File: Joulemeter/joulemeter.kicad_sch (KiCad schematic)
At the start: 42 parts, among them IC1 INA240A3PWR, J1 XT60-M, J2 XT60-M, J3 22035035, J4 22035035, U2 MCP6286T-E/OT, U5 PADS131M04QPWRQ1

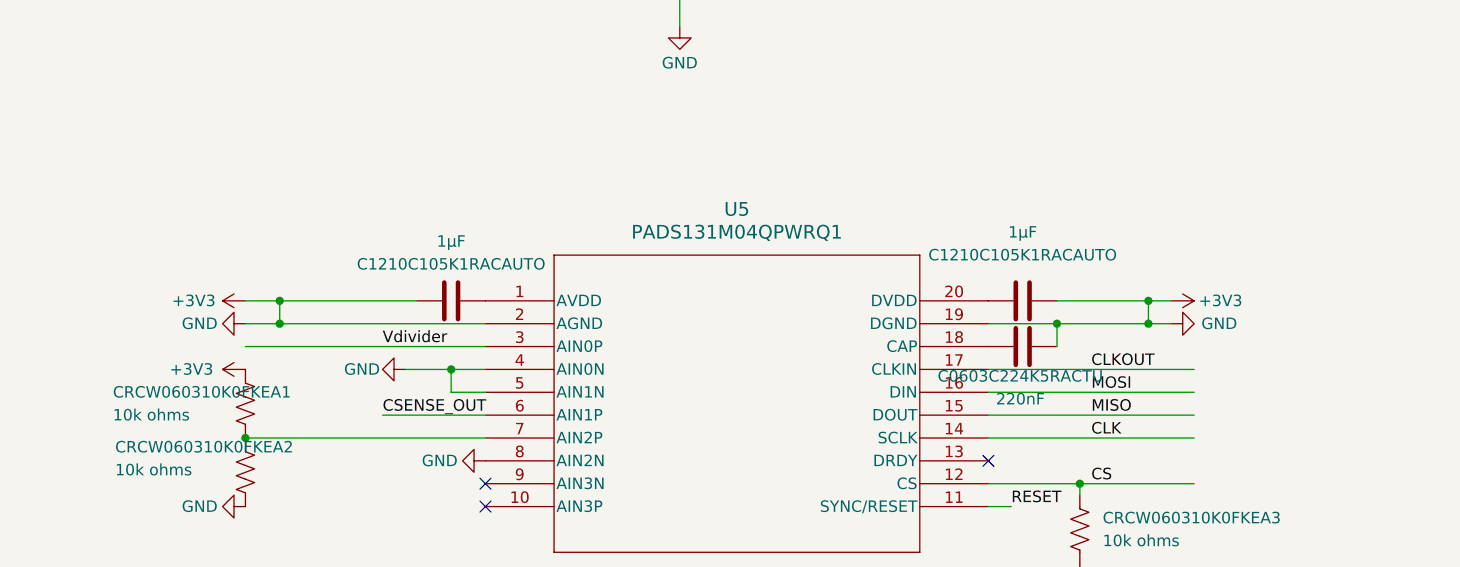
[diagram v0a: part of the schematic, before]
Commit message: fixed avdd agnd dvdd dgnd connections
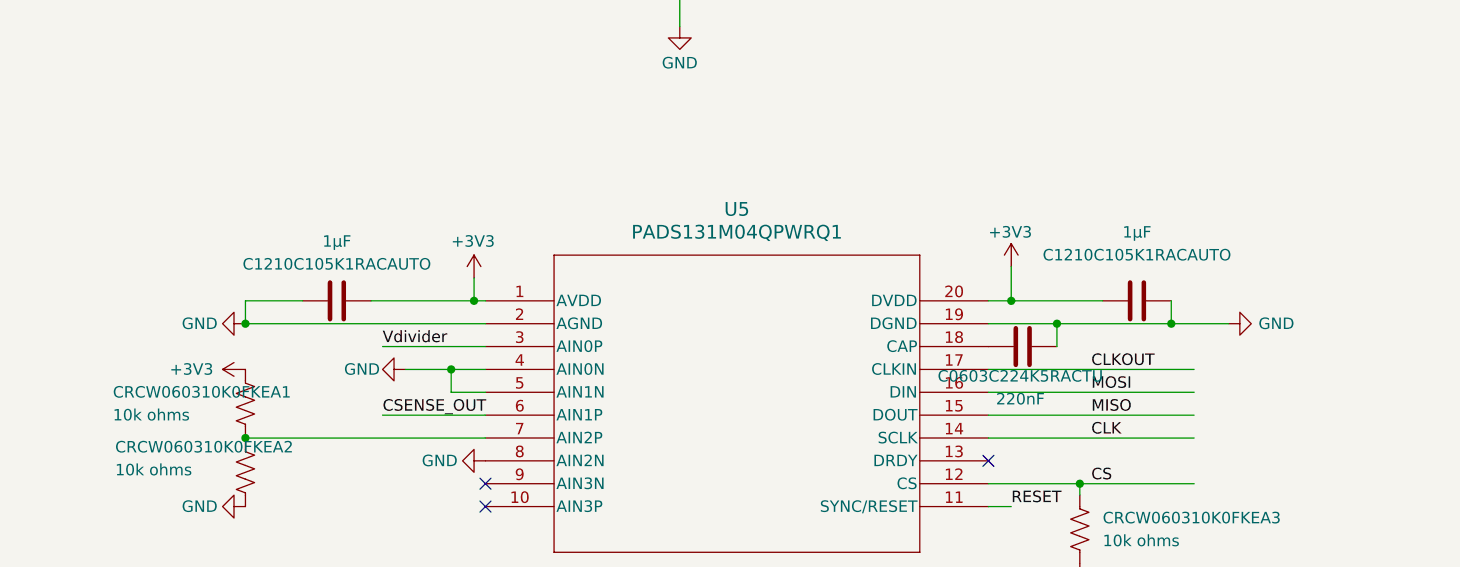
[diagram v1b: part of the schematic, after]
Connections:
- net +3V3: now also C1210C105K1RACAUTO.1, C1210C105K1RACAUTO.2, U5.1 (AVDD), U5.20 (DVDD); no longer C0603C224K5RACTU.2, C0603S223K5RACTU.1, C0805C475K4RACTU.2, C0805C475K4RACTU1.2, C1210C105K1RACAUTO.1, C1210C105K1RACAUTO.2, C1210C105K1RACAUTO.2, C1210C106K3RACAUTO.2, CRCW060310K0FKEA2.1, D1.1, IC1.4 (GND), IC1.7 (REF1), J1.N (NEG), J2.N (NEG), J3.2, J4.2, LDO1.4 (GND), RP2.13, RP2.2, TNPW080510K0BEEA.2, TP_GND.1, U2.2 (VSS), U5.19 (DGND), U5.2 (AGND), U5.4 (AIN0N), U5.5 (AIN1N), U5.8 (AIN2N)
- net GND: now reaches RP2.2
- net GND: now also C0603C224K5RACTU.2, C0603S223K5RACTU.1, C0805C475K4RACTU.2, C0805C475K4RACTU1.2, C1210C105K1RACAUTO.1, C1210C105K1RACAUTO.2, C1210C105K1RACAUTO.2, C1210C106K3RACAUTO.2, CRCW060310K0FKEA2.1, D1.1, IC1.4 (GND), IC1.7 (REF1), J1.N (NEG), J2.N (NEG), J3.2, J4.2, LDO1.4 (GND), RP2.13, TNPW080510K0BEEA.2, TP_GND.1, U2.2 (VSS), U5.19 (DGND), U5.2 (AGND), U5.4 (AIN0N), U5.5 (AIN1N), U5.8 (AIN2N)
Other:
- moved on the sheet: C1210C105K1RACAUTO

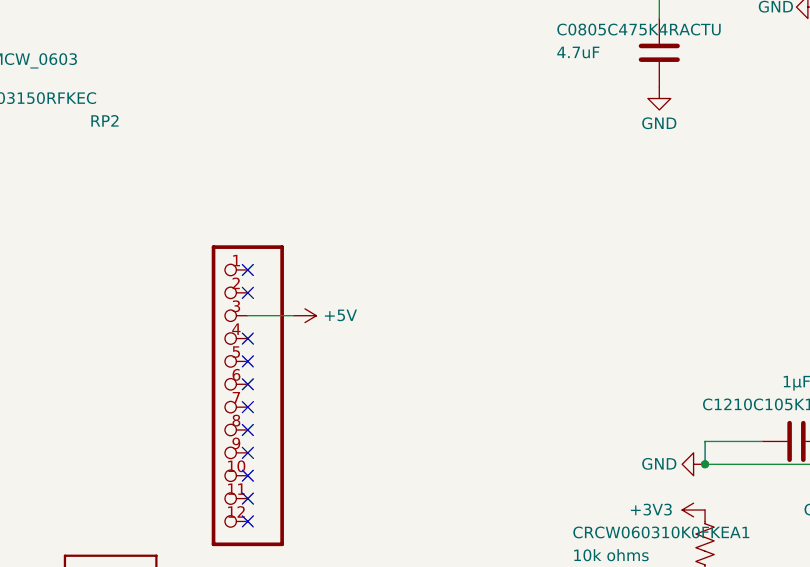
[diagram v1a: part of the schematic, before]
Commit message: bypass cap for rp2040
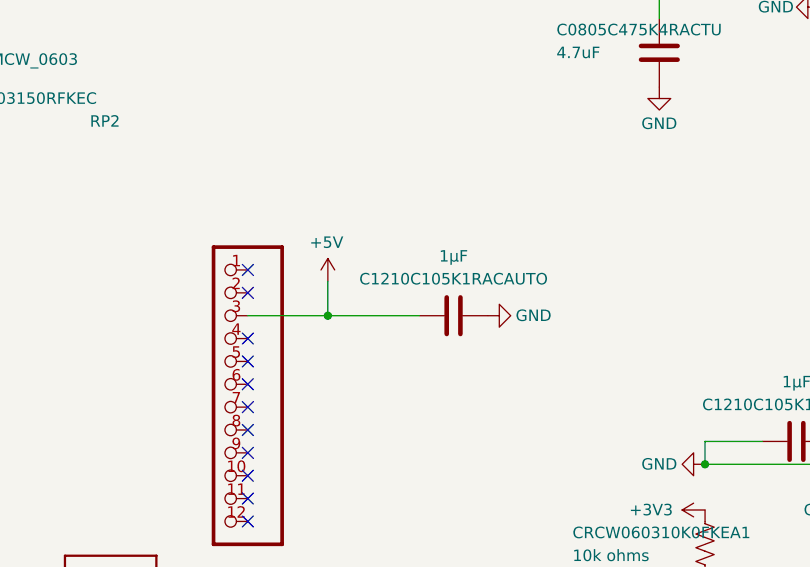
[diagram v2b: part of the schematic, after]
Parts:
- added C1210C105K1RACAUTO: 1μF, symbol Device:C
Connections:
- net +5V: now also C1210C105K1RACAUTO.1
- net GND: now also C1210C105K1RACAUTO.2
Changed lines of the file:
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@@
 	)
 	(junction
+		(at 85.09 106.68)
+		(diameter 0)
+		(color 0 0 0 0)
+	)
+	(junction
 		(at 212.09 120.65)
 		(diameter 0)
@@
 	(wire
 		(pts
+			(xy 76.2 106.68) (xy 85.09 106.68)
+		)
+		(stroke
+			(width 0)
+			(type default)
+		)
+	)
+	(wire
+		(pts
 			(xy 29.21 40.64) (xy 48.26 40.64)
 		)
@@
 	(wire
 		(pts
+			(xy 85.09 106.68) (xy 95.25 106.68)
+		)
+		(stroke
+			(width 0)
+			(type default)
+		)
+	)
+	(wire
+		(pts
 			(xy 127 135.89) (xy 153.67 135.89)
 		)
@@
 	(wire
 		(pts
-			(xy 118.11 175.26) (xy 115.57 175.26)
+			(xy 85.09 102.87) (xy 85.09 106.68)
 		)
 		(stroke
@@
 	(wire
 		(pts
-			(xy 229.87 123.19) (xy 217.17 123.19)
+			(xy 118.11 175.26) (xy 115.57 175.26)
 		)
 		(stroke
@@
 	(wire
 		(pts
-			(xy 29.21 35.56) (xy 29.21 40.64)
+			(xy 229.87 123.19) (xy 217.17 123.19)
 		)
 		(stroke
@@
 	(wire
 		(pts
-			(xy 76.2 106.68) (xy 81.28 106.68)
+			(xy 29.21 35.56) (xy 29.21 40.64)
 		)
 		(stroke
@@
 	)
 	(symbol
+		(lib_id "Device:C")
+		(at 99.06 106.68 90)
+		(unit 1)
+		(exclude_from_sim no)
+		(in_bom yes)
+		(on_board yes)
+		(dnp no)
+		(property "Reference" "C1210C105K1RACAUTO"
+			(at 99.06 102.616 90)
+			(effects
+				(font
+					(size 1.27 1.27)
+				)
+			)
+		)
+		(property "Value" "1μF"
+			(at 99.06 100.076 90)
+			(effects
+				(font
+					(size 1.27 1.27)
+				)
+			)
+		)
+		(property "Footprint" ""
+			(at 102.87 105.7148 0)
+			(effects
+				(font
+					(size 1.27 1.27)
+				)
+				(hide yes)
+			)
+		)
+		(property "Datasheet" "~"
+			(at 99.06 106.68 0)
+			(effects
+				(font
+					(size 1.27 1.27)
+				)
+				(hide yes)
+			)
+		)
+		(property "Description" "Unpolarized capacitor"
+			(at 99.06 106.68 0)
+			(effects
+				(font
+					(size 1.27 1.27)
+				)
+				(hide yes)
+			)
+		)
+		(pin "2"
+		)
+		(pin "1"
+		)
+		(instances
+			(project "joulemeter"
+				(path "/62c9b90f-facd-44d7-9ffc-18aee2f06026"
+					(reference "C1210C105K1RACAUTO")
+					(unit 1)
+				)
+			)
+		)
+	)
+	(symbol
 		(lib_id "power:GND")
 		(at 153.67 138.43 270)
@@
 	(symbol
 		(lib_id "power:GND")
+		(at 102.87 106.68 90)
+		(unit 1)
+		(exclude_from_sim no)
+		(in_bom yes)
+		(on_board yes)
+		(dnp no)
+		(property "Reference" "#PWR033"
+			(at 109.22 106.68 0)
+			(effects
+				(font
+					(size 1.27 1.27)
+				)
+				(hide yes)
+			)
+		)
+		(property "Value" "GND"
+			(at 107.95 106.68 90)
+			(effects
+				(font
+					(size 1.27 1.27)
+				)
+			)
+		)
+		(property "Footprint" ""
+			(at 102.87 106.68 0)
+			(effects
+				(font
+					(size 1.27 1.27)
+				)
+				(hide yes)
+			)
+		)
+		(property "Datasheet" ""
+			(at 102.87 106.68 0)
+			(effects
+				(font
+					(size 1.27 1.27)
+				)
+				(hide yes)
+			)
+		)
+		(property "Description" "Power symbol creates a global label with name \"GND\" , ground"
+			(at 102.87 106.68 0)
+			(effects
+				(font
+					(size 1.27 1.27)
+				)
+				(hide yes)
+			)
+		)
+		(pin "1"
+		)
+		(instances
+			(project "joulemeter"
+				(path "/62c9b90f-facd-44d7-9ffc-18aee2f06026"
+					(reference "#PWR033")
+					(unit 1)
+				)
+			)
+		)
+	)
+	(symbol
+		(lib_id "power:GND")
 		(at 236.22 123.19 90)
 		(unit 1)
@@
 	(symbol
 		(lib_id "power:+5V")
-		(at 81.28 106.68 270)
+		(at 85.09 102.87 0)
 		(unit 1)
 		(exclude_from_sim no)
@@
 		(dnp no)
 		(property "Reference" "#PWR010"
-			(at 77.47 106.68 0)
+			(at 85.09 106.68 0)
 			(effects
 				(font
@@
 		)
 		(property "Value" "+5V"
-			(at 84.582 106.68 90)
+			(at 83.058 98.552 0)
 			(effects
 				(font
@@
 		)
 		(property "Footprint" ""
-			(at 81.28 106.68 0)
+			(at 85.09 102.87 0)
 			(effects
 				(font
@@
 		)
 		(property "Datasheet" ""
-			(at 81.28 106.68 0)
+			(at 85.09 102.87 0)
 			(effects
 				(font
@@
 		)
 		(property "Description" "Power symbol creates a global label with name \"+5V\""
-			(at 81.28 106.68 0)
+			(at 85.09 102.87 0)
 			(effects
 				(font

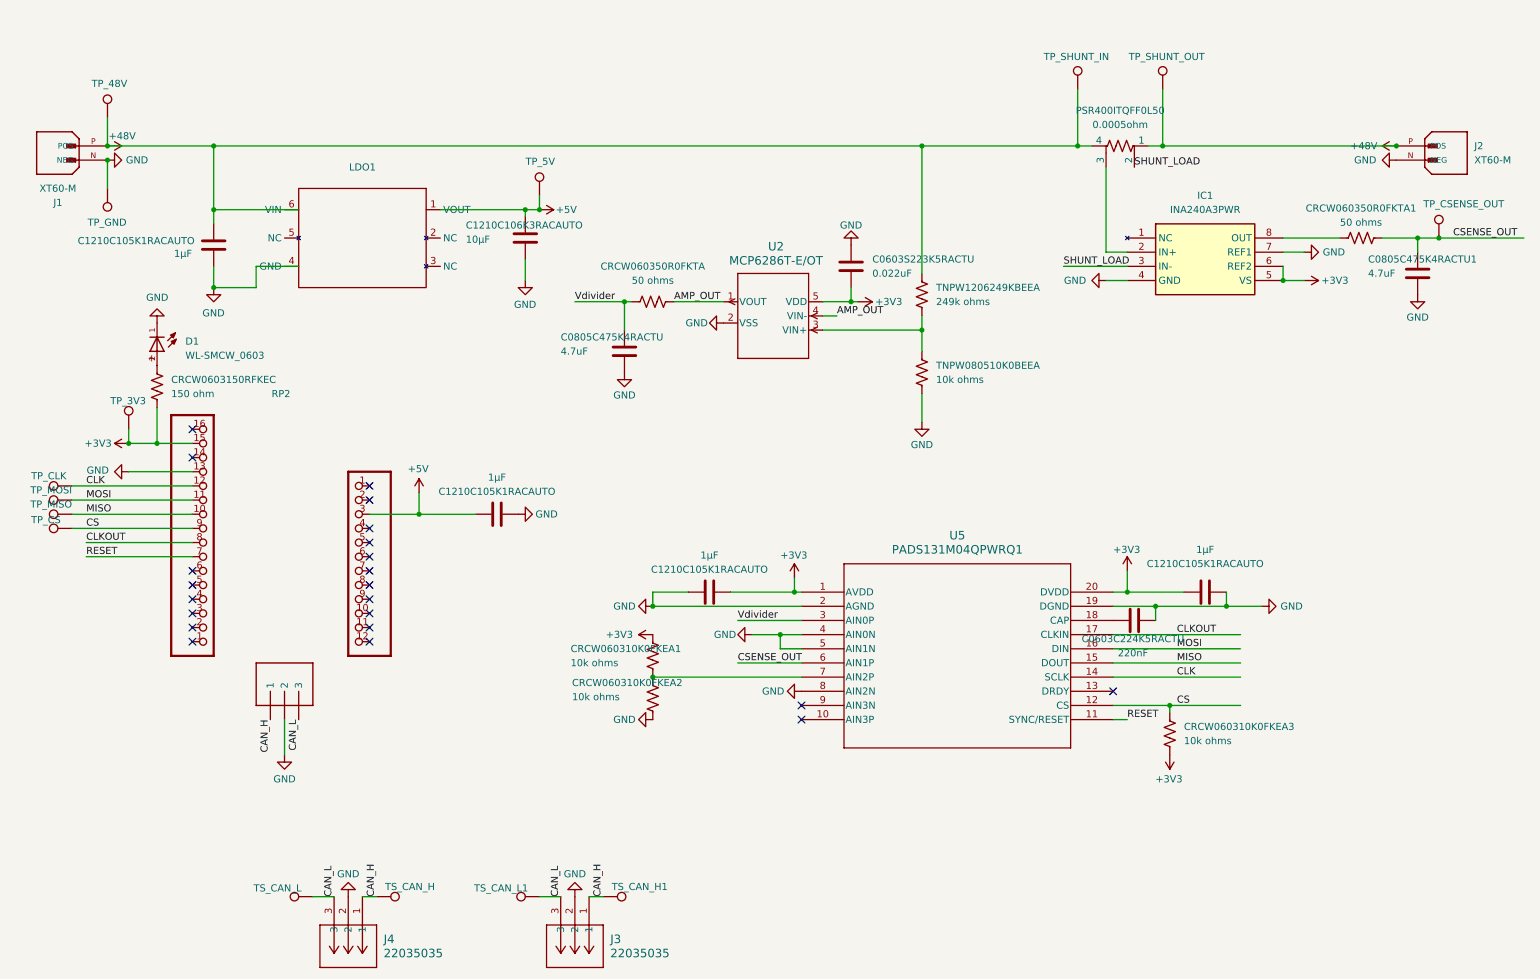
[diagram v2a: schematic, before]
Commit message: replaced ina240 with custom symbol
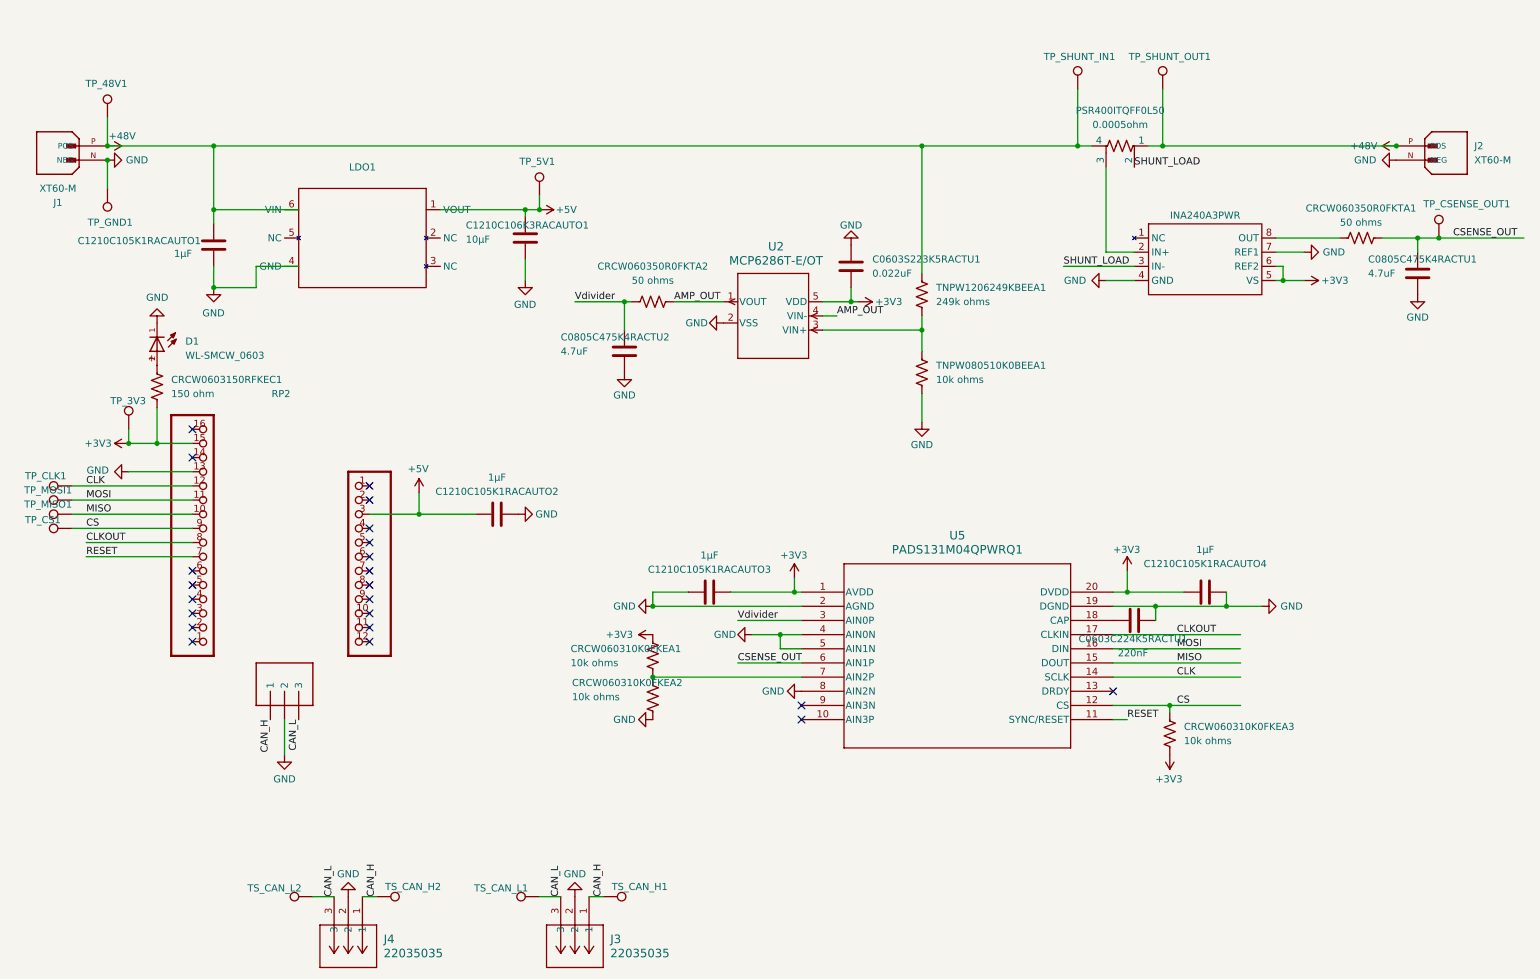
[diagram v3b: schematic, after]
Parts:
- removed IC1: INA240A3PWR, SOP65P640X120-8N, symbol INA240A3PWR:INA240A3PWR
- added INA240A3PWR: ~, SMV_ICs:SOP65P640X120-8N, symbol SMV_Custom:INA240A3PWR
- renumbered C0603C224K5RACTU to C0603C224K5RACTU1, C0603S223K5RACTU to C0603S223K5RACTU1, C0805C475K4RACTU to C0805C475K4RACTU2, C1210C105K1RACAUTO to C1210C105K1RACAUTO1, C1210C105K1RACAUTO to C1210C105K1RACAUTO2, C1210C105K1RACAUTO to C1210C105K1RACAUTO3, C1210C105K1RACAUTO to C1210C105K1RACAUTO4, C1210C106K3RACAUTO to C1210C106K3RACAUTO1, CRCW0603150RFKEC to CRCW0603150RFKEC1, CRCW060350R0FKTA to CRCW060350R0FKTA2, TNPW080510K0BEEA to TNPW080510K0BEEA1, TNPW1206249KBEEA to TNPW1206249KBEEA1, TP_48V to TP_48V1, TP_5V to TP_5V1, TP_CLK to TP_CLK1, TP_CS to TP_CS1, TP_CSENSE_OUT to TP_CSENSE_OUT1, TP_GND to TP_GND1, TP_MISO to TP_MISO1, TP_MOSI to TP_MOSI1, TP_SHUNT_IN to TP_SHUNT_IN1, TP_SHUNT_OUT to TP_SHUNT_OUT1, TS_CAN_H to TS_CAN_H2, TS_CAN_L to TS_CAN_L2
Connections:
- net +3V3: now also INA240A3PWR.5 (VS), INA240A3PWR.6 (REF2)
- net GND: now also INA240A3PWR.4 (GND), INA240A3PWR.7 (REF1)
- net SHUNT_LOAD: now also INA240A3PWR.3 (IN-)
- net at PSR400ITQFF0L50.3: now also INA240A3PWR.2 (IN+)
- net at CRCW060350R0FKTA1.1: now also INA240A3PWR.8 (OUT)

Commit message: pcb
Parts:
- removed TP_SHUNT_OUT1: ~, symbol Connector:TestPoint
- added C3: 0.1uF,50V, SMV_Passives:Cap0805, symbol SMV_Custom:C0805C104K5RACTU
- added C70, C71: 470uF, 63V, SMV_Passives:Big_Chunky_Cap, symbol SMV_Custom:Big_Chunky_Cap2
- added C72, C74: C2220C475M1R2C7186, SMV_Passives:CAP_C2220C_2S_KEM-L, symbol SMV_Custom:C2220C475M1R2C7186
- added R10, R70: R_US, Resistor_THT:R_Axial_DIN0204_L3.6mm_D1.6mm_P1.90mm_Vertical, symbol Device:R_US
- added TP_SHUNT_OUT2: ~, TestPoint:TestPoint_Pad_D2.5mm, symbol Connector:TestPoint
- C0603C224K5RACTU1, C0603S223K5RACTU1: footprint (none) -> SMV_Passives:CAPC17595_87N_KEM-L
- C0805C475K4RACTU1, C0805C475K4RACTU2: footprint (none) -> SMV_Passives:Cap0805
- C1210C105K1RACAUTO1, C1210C105K1RACAUTO2, C1210C105K1RACAUTO3, C1210C105K1RACAUTO4, C1210C106K3RACAUTO1: footprint (none) -> SMV_Passives:CAPC340270_190N_KEM-M
- CRCW060310K0FKEA1, CRCW060310K0FKEA2, CRCW060310K0FKEA3, CRCW0603150RFKEC1, CRCW060350R0FKTA1, CRCW060350R0FKTA2: footprint (none) -> SMV_Passives:RESC1608X50N
- J1, J2: footprint XT60-M:AMASS_XT60-M -> SMV_Connectors:AMASS_XT60-M
- J3, J4: footprint CON_22035035_MOL -> SMV_Connectors:3pin_CON_22035035_MOL
- LDO1: footprint (none) -> SMV_ICs:U-DFN2020-6_TYPE-C_DIO-M
- PSR400ITQFF0L50: footprint (none) -> SMV_Passives:RES_PSR400IT_ROM-L
- RP2: footprint (none) -> SMV_Connectors:RP2040
- TNPW080510K0BEEA1: footprint (none) -> SMV_Passives:0805RESC2012X60N
- TNPW1206249KBEEA1: footprint (none) -> SMV_Passives:RES_TNPW1206_VIS-M
- TP_3V3, TP_48V1, TP_5V1, TP_CLK1, TP_CS1, TP_CSENSE_OUT1, TP_GND1, TP_MISO1, TP_MOSI1, TP_SHUNT_IN1, TS_CAN_H1, TS_CAN_H2, TS_CAN_L1, TS_CAN_L2: footprint (none) -> TestPoint:TestPoint_Pad_D2.5mm
- renumbered INA240A3PWR to INA240A3PWR1
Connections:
- net +3V3: now also RP2.26, RP2.27, C3.1; no longer RP2.15
- net +48V: now also C71.2, C72.1; no longer J2.P (POS), PSR400ITQFF0L50.1
- net +5V: now also LDO1.1 (VOUT)
- net CS: now also RP2.21; no longer RP2.9
- net CSENSE_OUT: now also U5.3 (AIN0P); no longer U5.6 (AIN1P)
- net GND: now also RP2.25, U5.6 (AIN1P), U5.9 (AIN3N), C3.2, C72.2, C74.2, R10.1, R70.1; no longer RP2.13
- net MISO: now also RP2.22; no longer RP2.10
- net MOSI: now also RP2.23; no longer RP2.11
- net RESET: now also RP2.20; no longer RP2.7
- net Vdivider: now also U5.10 (AIN3P); no longer U5.3 (AIN0P)
- removed net CLK: RP2.12, TP_CLK1.1, U5.14 (SCLK)
- net CLKOUT renamed GPIO_CLKIN
- net GPIO_CLKIN: now also RP2.24, TP_CLK1.1; no longer RP2.8
- new net: C70.2, C74.1, J2.P (POS), PSR400ITQFF0L50.1, TP_SHUNT_OUT2.1
- new net: C71.1, R10.2
- new net: C70.1, R70.2
- new net SCK: RP2.18, U5.14 (SCLK)
- no-connect marks 22 -> 19
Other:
- moved on the sheet: CRCW060310K0FKEA1, CRCW060310K0FKEA2, PSR400ITQFF0L50

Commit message: pcb 3
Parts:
- C1: renamed from C72; value C2220C475M1R2C7186 -> 4.7 µF
- C10: renamed from C1210C105K1RACAUTO2; value 1μF -> 1 µF
- C4: renamed from C74; value C2220C475M1R2C7186 -> 4.7 µF
- renumbered C1210C105K1RACAUTO3 to C11, C1210C105K1RACAUTO4 to C12, C0603C224K5RACTU1 to C13, C3 to C14, C71 to C2, C70 to C3, C1210C105K1RACAUTO1 to C5, C1210C106K3RACAUTO1 to C6, C0603S223K5RACTU1 to C7, C0805C475K4RACTU2 to C8, C0805C475K4RACTU1 to C9, R10 to R1, CRCW060310K0FKEA3 to R10, R70 to R2, CRCW060350R0FKTA2 to R3, TNPW1206249KBEEA1 to R4, TNPW080510K0BEEA1 to R5, CRCW060350R0FKTA1 to R6, CRCW0603150RFKEC1 to R7, CRCW060310K0FKEA1 to R8, CRCW060310K0FKEA2 to R9, PSR400ITQFF0L50 to R_shunt1

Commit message: helllo
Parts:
- C1, C4: footprint SMV_Passives:CAP_C2220C_2S_KEM-L -> SMV_Passives:CAPC340180_180N_KEM
- C10, C11, C12, C5, C6: footprint SMV_Passives:CAPC340270_190N_KEM-M -> SMV_Passives:Cap0805
- C13: footprint SMV_Passives:CAPC17595_87N_KEM-L -> SMV_Passives:Cap0805
- C7: value 0.022uF -> 0.1uF; footprint SMV_Passives:CAPC17595_87N_KEM-L -> SMV_Passives:Cap0805
- C8, C9: value 4.7uF -> 4.7nF; footprint SMV_Passives:Cap0805 -> SMV_Passives:CAPC17595_87N_KEM
- R10, R8, R9: value 10k ohms -> 20k ohms; footprint SMV_Passives:RESC1608X50N -> SMV_Passives:0603_resistors
- R3, R6, R7: footprint SMV_Passives:RESC1608X50N -> SMV_Passives:0805RESC2012X60N
- R4: value 249k ohms -> 500k ohms; footprint SMV_Passives:RES_TNPW1206_VIS-M -> SMV_Passives:0805RESC2012X60N
- R5: value 10k ohms -> 20k ohms; footprint SMV_Passives:0805RESC2012X60N -> SMV_Passives:0603_resistors
